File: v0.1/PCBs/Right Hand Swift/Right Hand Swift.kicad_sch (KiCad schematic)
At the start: 18 parts, among them J1 FFC Connector

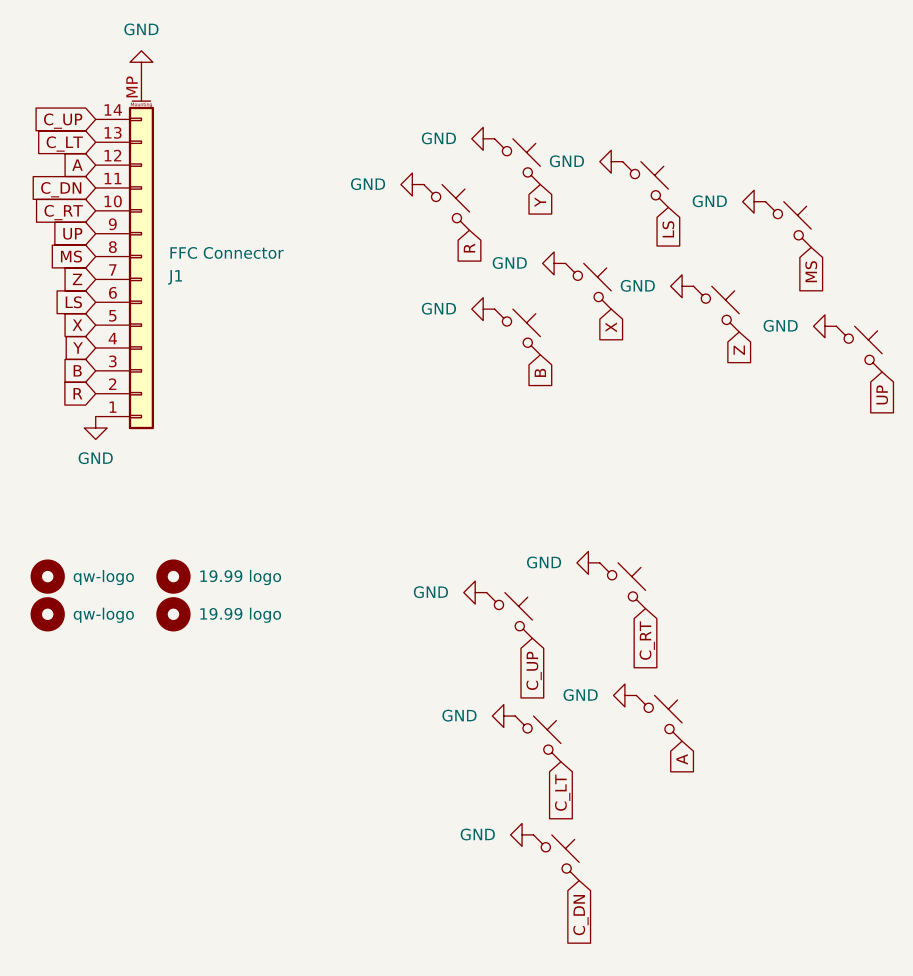
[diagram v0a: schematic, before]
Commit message: Adjusted Swift right side to the preferred footprint
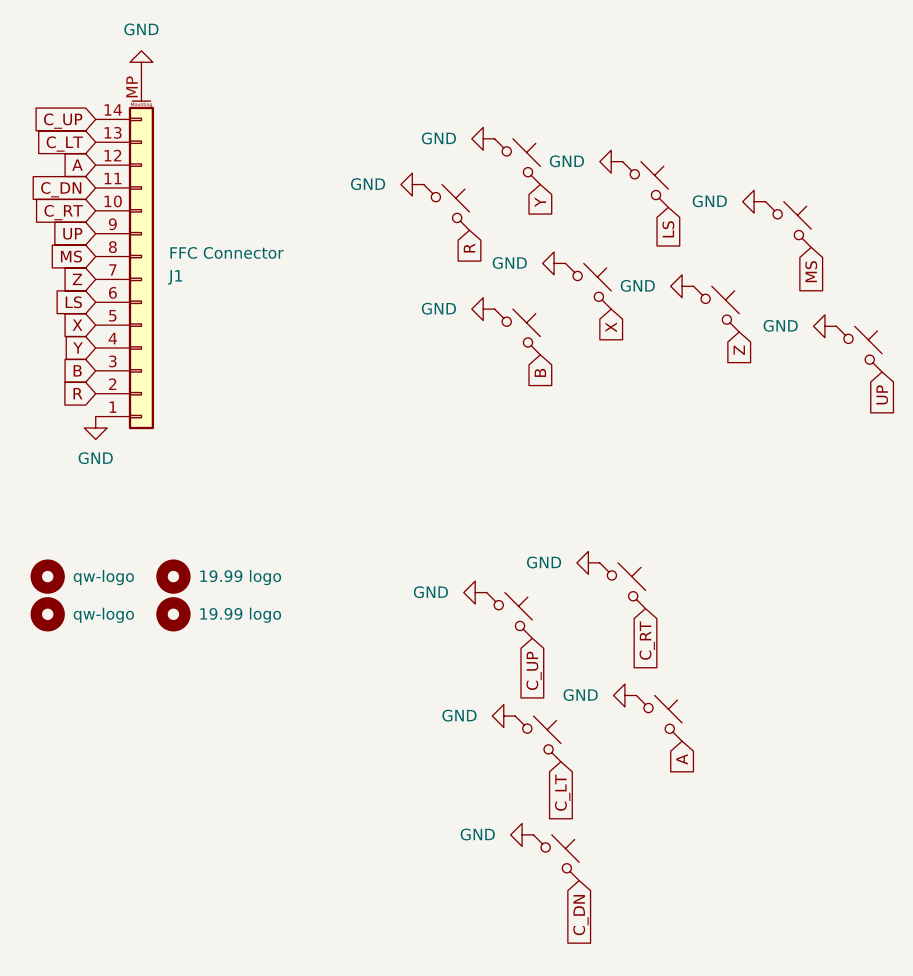
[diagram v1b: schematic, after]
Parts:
- CH10, CH11, CH12, CH13, CH14, CH15, CH16, CH17, CH18, CH19, CH20, CH8, CH9: footprint PCM_marbastlib-choc:SW_choc_v1_HS_1u -> PCBs:Kailh_socket_PG1350
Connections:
- net A: now also CH17.1; no longer CH17.2
- net B: now also CH11.1; no longer CH11.2
- net C_DN: now also CH13.1; no longer CH13.2
- net C_LT: now also CH12.1; no longer CH12.2
- net C_RT: now also CH15.1; no longer CH15.2
- net C_UP: now also CH9.1; no longer CH9.2
- net GND: now also CH10.2, CH11.2, CH12.2, CH13.2, CH14.2, CH15.2, CH16.2, CH17.2, CH18.2, CH19.2, CH20.2, CH8.2, CH9.2; no longer CH10.1, CH11.1, CH12.1, CH13.1, CH14.1, CH15.1, CH16.1, CH17.1, CH18.1, CH19.1, CH20.1, CH8.1, CH9.1
- net LS: now also CH16.1; no longer CH16.2
- net MS: now also CH19.1; no longer CH19.2
- net R: now also CH8.1; no longer CH8.2
- net UP: now also CH20.1; no longer CH20.2
- net X: now also CH14.1; no longer CH14.2
- net Y: now also CH10.1; no longer CH10.2
- net Z: now also CH18.1; no longer CH18.2
